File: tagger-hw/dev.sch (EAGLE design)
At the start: 40 parts, among them IC1 4010D, IC2 LP298XS, J1 SMARTPRJ_MYCON2_USB-MINI-B, X1 MICROSD, X2 22-23-2021, X3 22-23-2021

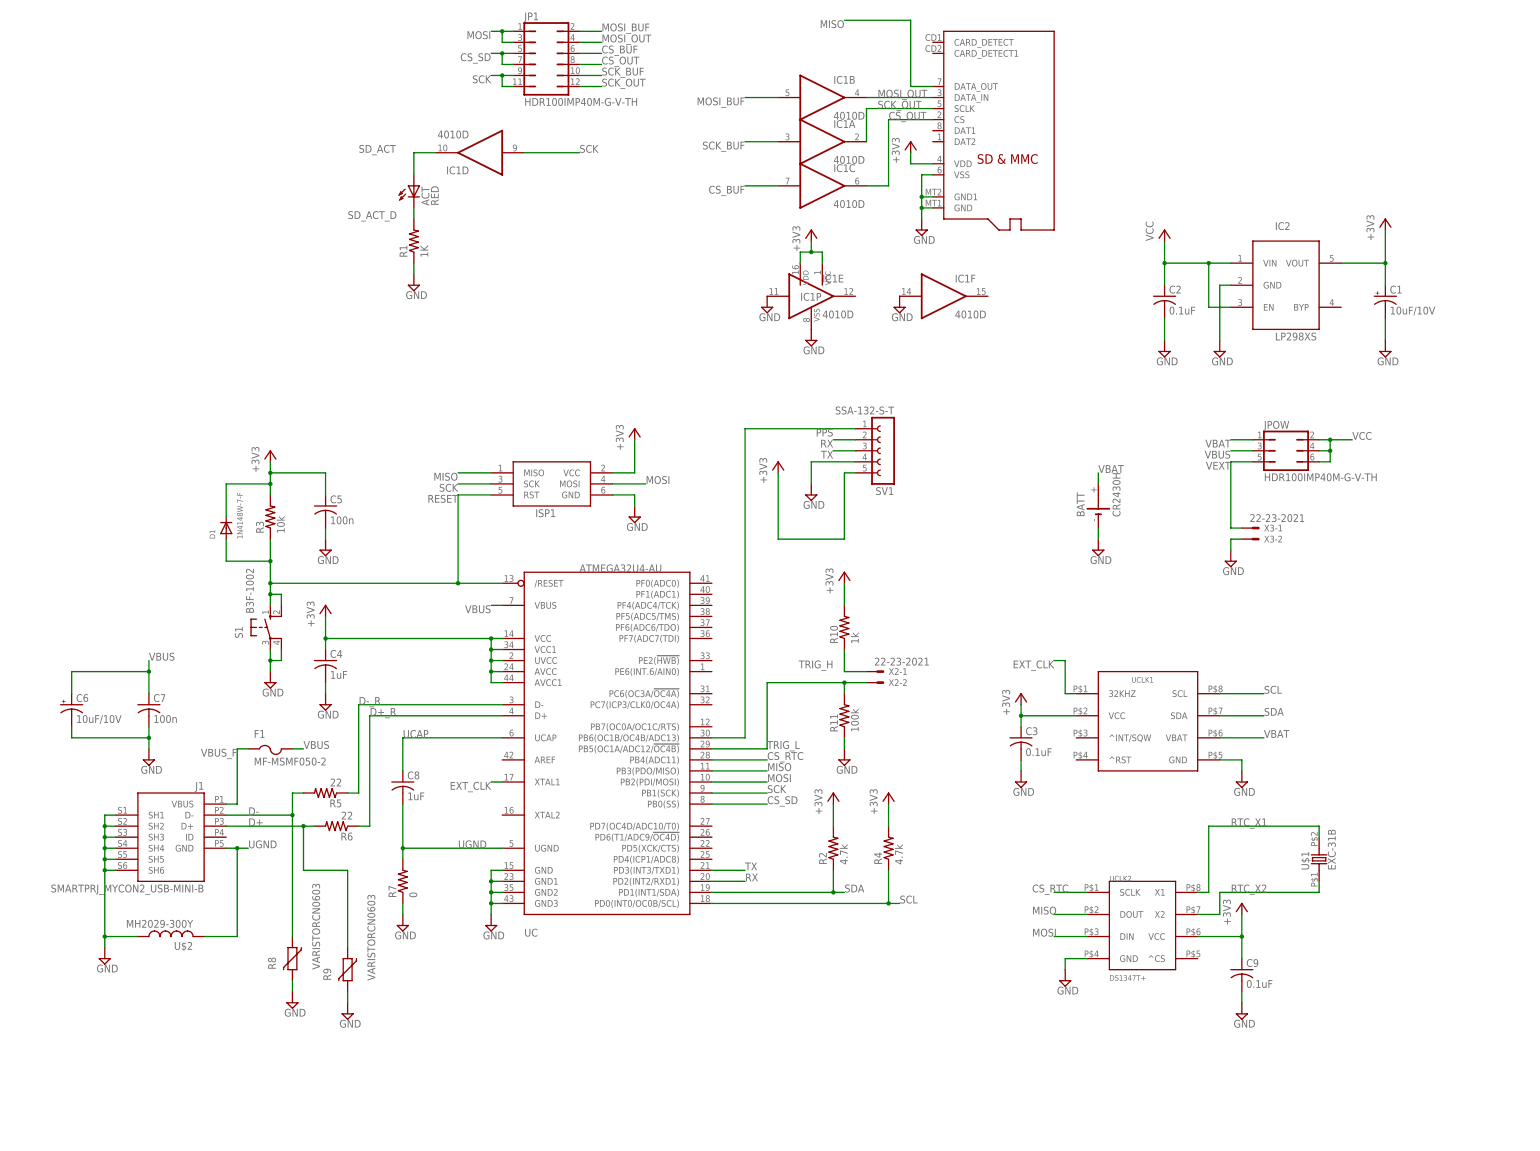
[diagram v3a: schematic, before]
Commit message: Just kidding, add more buttons and LEDs
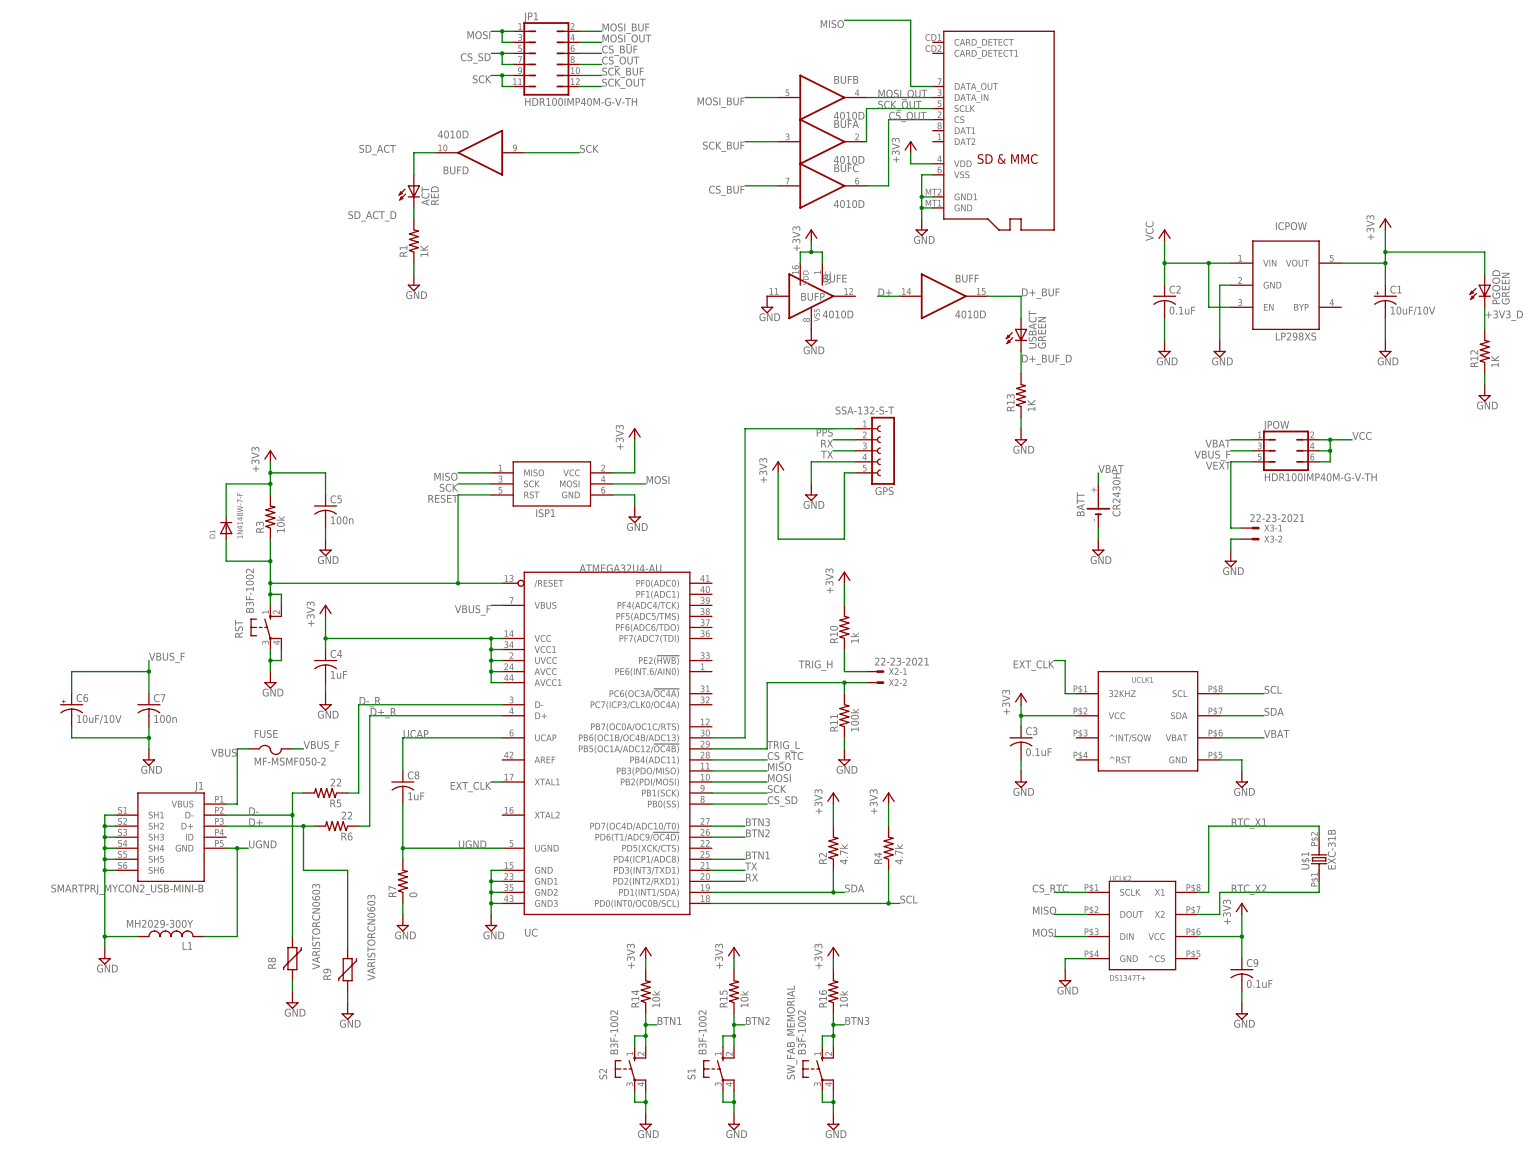
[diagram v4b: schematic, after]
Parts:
- added PGOOD, USBACT: GREEN, adafruit:LEDCHIP-LED0805
- added R12, R13: 1K, adafruit:R-US_R0805
- added R14, R15, R16: 10k, resistor:R-US_R0603
- added RST, S2, SW_FAB_MEMORIAL: B3F-1002, switch-omron:10-XX
- renumbered F1 to FUSE, IC1 to BUF, IC2 to ICPOW, SV1 to GPS, U$2 to L1, X1 to SD
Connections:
- new net +3V3_D: PGOOD.C, R12.2
- new net BTN1: R14.1, S2.S, S2.S1, UC.PD4(ICP1/ADC8)
- new net BTN2: R15.1, S1.S, S1.S1, UC.PD6(T1/ADC9/!OC4D)
- new net BTN3: R16.1, SW_FAB_MEMORIAL.S, SW_FAB_MEMORIAL.S1, UC.PD7(OC4D/ADC10/T0)
- new net D+_BUF: BUFF.O, USBACT.A
- new net D+_BUF_D: R13.2, USBACT.C
- net +3V3: now also PGOOD.A, R14.2, R15.2, R16.2
- net D+: now also BUFF.I
- net GND: now also R12.1, R13.1, RST.P, RST.P1, S2.P, S2.P1, SW_FAB_MEMORIAL.P, SW_FAB_MEMORIAL.P1; no longer BUFF.I
- net RESET: now also RST.S, RST.S1; no longer S1.S, S1.S1
- net VBUS: now also FUSE.1, J1.VBUS; no longer C6.+, C7.1, FUSE.2, JPOW.3, UC.VBUS
- net VBUS_F: now also C6.+, C7.1, FUSE.2, JPOW.3, UC.VBUS; no longer FUSE.1, J1.VBUS
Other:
- moved on the sheet: S1

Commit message: Minor name changes
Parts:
- renumbered U$1 to X1, X2 to J2, X3 to J3
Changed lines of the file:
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@@
 <part name="SUPPLY23" library="supply2" library_urn="urn:adsk.eagle:library:372" deviceset="GND" device=""/>
 <part name="+3V10" library="supply1" library_urn="urn:adsk.eagle:library:371" deviceset="+3V3" device=""/>
-<part name="U$1" library="dorskyee" deviceset="EXC-31B" device=""/>
-<part name="X2" library="con-molex" library_urn="urn:adsk.eagle:library:165" deviceset="22-23-2021" device=""/>
+<part name="X1" library="dorskyee" deviceset="EXC-31B" device=""/>
+<part name="J2" library="con-molex" library_urn="urn:adsk.eagle:library:165" deviceset="22-23-2021" device=""/>
 <part name="R10" library="resistor" library_urn="urn:adsk.eagle:library:348" deviceset="R-US_" device="R0603" package3d_urn="urn:adsk.eagle:package:26057/1" value="1k"/>
 <part name="+3V11" library="supply1" library_urn="urn:adsk.eagle:library:371" deviceset="+3V3" device=""/>
 <part name="R11" library="resistor" library_urn="urn:adsk.eagle:library:348" deviceset="R-US_" device="R0603" package3d_urn="urn:adsk.eagle:package:26057/1" value="100k"/>
 <part name="SUPPLY24" library="supply2" library_urn="urn:adsk.eagle:library:372" deviceset="GND" device=""/>
-<part name="X3" library="con-molex" library_urn="urn:adsk.eagle:library:165" deviceset="22-23-2021" device=""/>
+<part name="J3" library="con-molex" library_urn="urn:adsk.eagle:library:165" deviceset="22-23-2021" device=""/>
 <part name="SUPPLY25" library="supply2" library_urn="urn:adsk.eagle:library:372" deviceset="GND" device=""/>
 <part name="L1" library="dorskyee" deviceset="MH2029-300Y" device=""/>
@@
 <instance part="SUPPLY23" gate="GND" x="116.84" y="-129.54"/>
 <instance part="+3V10" gate="G$1" x="116.84" y="-104.14"/>
-<instance part="U$1" gate="G$1" x="134.62" y="-93.98" rot="R90"/>
-<instance part="X2" gate="-1" x="33.02" y="-50.8"/>
-<instance part="X2" gate="-2" x="33.02" y="-53.34"/>
+<instance part="X1" gate="G$1" x="134.62" y="-93.98" rot="R90"/>
+<instance part="J2" gate="-1" x="33.02" y="-50.8"/>
+<instance part="J2" gate="-2" x="33.02" y="-53.34"/>
 <instance part="R10" gate="G$1" x="25.4" y="-40.64" rot="R90"/>
 <instance part="+3V11" gate="G$1" x="25.4" y="-27.94"/>
 <instance part="R11" gate="G$1" x="25.4" y="-60.96" rot="R90"/>
 <instance part="SUPPLY24" gate="GND" x="25.4" y="-71.12"/>
-<instance part="X3" gate="-1" x="119.38" y="-17.78"/>
-<instance part="X3" gate="-2" x="119.38" y="-20.32"/>
+<instance part="J3" gate="-1" x="119.38" y="-17.78"/>
+<instance part="J3" gate="-2" x="119.38" y="-20.32"/>
 <instance part="SUPPLY25" gate="GND" x="114.3" y="-25.4"/>
 <instance part="L1" gate="G$1" x="-129.54" y="-111.76" rot="R90"/>
@@
 </segment>
 <segment>
-<pinref part="X3" gate="-2" pin="S"/>
+<pinref part="J3" gate="-2" pin="S"/>
 <pinref part="SUPPLY25" gate="GND" pin="GND"/>
 <wire x1="116.84" y1="-20.32" x2="114.3" y2="-20.32" width="0.1524" layer="91"/>
@@
 <wire x1="114.3" y1="-2.54" x2="119.38" y2="-2.54" width="0.1524" layer="91"/>
 <label x="114.3" y="-2.54" size="1.778" layer="95" rot="R180"/>
-<pinref part="X3" gate="-1" pin="S"/>
+<pinref part="J3" gate="-1" pin="S"/>
 <wire x1="116.84" y1="-17.78" x2="114.3" y2="-17.78" width="0.1524" layer="91"/>
 <wire x1="114.3" y1="-17.78" x2="114.3" y2="-2.54" width="0.1524" layer="91"/>
@@
 <wire x1="111.76" y1="-106.68" x2="111.76" y2="-101.6" width="0.1524" layer="91"/>
 <wire x1="111.76" y1="-101.6" x2="134.62" y2="-101.6" width="0.1524" layer="91"/>
-<pinref part="U$1" gate="G$1" pin="1"/>
+<pinref part="X1" gate="G$1" pin="1"/>
 <wire x1="134.62" y1="-101.6" x2="134.62" y2="-99.06" width="0.1524" layer="91"/>
 <label x="114.3" y="-101.6" size="1.778" layer="95"/>
@@
 <wire x1="109.22" y1="-101.6" x2="109.22" y2="-86.36" width="0.1524" layer="91"/>
 <wire x1="109.22" y1="-86.36" x2="134.62" y2="-86.36" width="0.1524" layer="91"/>
-<pinref part="U$1" gate="G$1" pin="2"/>
+<pinref part="X1" gate="G$1" pin="2"/>
 <wire x1="134.62" y1="-86.36" x2="134.62" y2="-88.9" width="0.1524" layer="91"/>
 <label x="114.3" y="-86.36" size="1.778" layer="95"/>
@@
 <net name="TRIG_L" class="0">
 <segment>
-<pinref part="X2" gate="-2" pin="S"/>
+<pinref part="J2" gate="-2" pin="S"/>
 <wire x1="30.48" y1="-53.34" x2="25.4" y2="-53.34" width="0.1524" layer="91"/>
 <wire x1="25.4" y1="-53.34" x2="25.4" y2="-55.88" width="0.1524" layer="91"/>
@@
 <segment>
 <pinref part="R10" gate="G$1" pin="1"/>
-<pinref part="X2" gate="-1" pin="S"/>
+<pinref part="J2" gate="-1" pin="S"/>
 <wire x1="30.48" y1="-50.8" x2="25.4" y2="-50.8" width="0.1524" layer="91"/>
 <wire x1="25.4" y1="-50.8" x2="25.4" y2="-45.72" width="0.1524" layer="91"/>

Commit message: More renaming
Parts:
- ICPOW: value LP298XS -> CAT6219-330TDGT3
- renumbered J1 to JUSB
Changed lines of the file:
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@@
 <part name="SUPPLY3" library="supply2" library_urn="urn:adsk.eagle:library:372" deviceset="GND" device=""/>
 <part name="+3V3" library="supply1" library_urn="urn:adsk.eagle:library:371" deviceset="+3V3" device=""/>
-<part name="ICPOW" library="adafruit" deviceset="LP298X" device="S"/>
+<part name="ICPOW" library="adafruit" deviceset="LP298X" device="S" value="CAT6219-330TDGT3"/>
 <part name="P+2" library="supply1" library_urn="urn:adsk.eagle:library:371" deviceset="VCC" device=""/>
 <part name="SUPPLY1" library="supply2" library_urn="urn:adsk.eagle:library:372" deviceset="GND" device=""/>
@@
 <part name="SUPPLY16" library="supply2" library_urn="urn:adsk.eagle:library:372" deviceset="GND" device=""/>
 <part name="JPOW" library="jumper" library_urn="urn:adsk.eagle:library:252" deviceset="JP3Q" device="" package3d_urn="urn:adsk.eagle:package:15460/1" value="HDR100IMP40M-G-V-TH"/>
-<part name="J1" library="dorskyee" deviceset="SMARTPRJ_MYCON2_USB-MINI-B" device=""/>
+<part name="JUSB" library="dorskyee" deviceset="SMARTPRJ_MYCON2_USB-MINI-B" device=""/>
 <part name="SUPPLY17" library="supply2" library_urn="urn:adsk.eagle:library:372" deviceset="GND" device=""/>
 <part name="R5" library="resistor" library_urn="urn:adsk.eagle:library:348" deviceset="R-US_" device="R0603" package3d_urn="urn:adsk.eagle:package:26057/1" value="22"/>
@@
 <instance part="SUPPLY16" gate="GND" x="83.82" y="-22.86"/>
 <instance part="JPOW" gate="B" x="127" y="0" rot="R270"/>
-<instance part="J1" gate="G$1" x="-129.54" y="-86.36" rot="MR0"/>
+<instance part="JUSB" gate="G$1" x="-129.54" y="-86.36" rot="MR0"/>
 <instance part="SUPPLY17" gate="GND" x="-144.78" y="-116.84"/>
 <instance part="R5" gate="G$1" x="-93.98" y="-78.74" rot="R180"/>
@@
 </segment>
 <segment>
-<pinref part="J1" gate="G$1" pin="SH6"/>
+<pinref part="JUSB" gate="G$1" pin="SH6"/>
 <pinref part="SUPPLY17" gate="GND" pin="GND"/>
 <wire x1="-142.24" y1="-96.52" x2="-144.78" y2="-96.52" width="0.1524" layer="91"/>
 <wire x1="-144.78" y1="-96.52" x2="-144.78" y2="-111.76" width="0.1524" layer="91"/>
-<pinref part="J1" gate="G$1" pin="SH5"/>
+<pinref part="JUSB" gate="G$1" pin="SH5"/>
 <wire x1="-144.78" y1="-111.76" x2="-144.78" y2="-114.3" width="0.1524" layer="91"/>
 <wire x1="-142.24" y1="-93.98" x2="-144.78" y2="-93.98" width="0.1524" layer="91"/>
 <wire x1="-144.78" y1="-93.98" x2="-144.78" y2="-96.52" width="0.1524" layer="91"/>
 <junction x="-144.78" y="-96.52"/>
-<pinref part="J1" gate="G$1" pin="SH4"/>
+<pinref part="JUSB" gate="G$1" pin="SH4"/>
 <wire x1="-142.24" y1="-91.44" x2="-144.78" y2="-91.44" width="0.1524" layer="91"/>
 <wire x1="-144.78" y1="-91.44" x2="-144.78" y2="-93.98" width="0.1524" layer="91"/>
 <junction x="-144.78" y="-93.98"/>
-<pinref part="J1" gate="G$1" pin="SH3"/>
+<pinref part="JUSB" gate="G$1" pin="SH3"/>
 <wire x1="-142.24" y1="-88.9" x2="-144.78" y2="-88.9" width="0.1524" layer="91"/>
 <wire x1="-144.78" y1="-88.9" x2="-144.78" y2="-91.44" width="0.1524" layer="91"/>
 <junction x="-144.78" y="-91.44"/>
-<pinref part="J1" gate="G$1" pin="SH2"/>
+<pinref part="JUSB" gate="G$1" pin="SH2"/>
 <wire x1="-142.24" y1="-86.36" x2="-144.78" y2="-86.36" width="0.1524" layer="91"/>
 <wire x1="-144.78" y1="-86.36" x2="-144.78" y2="-88.9" width="0.1524" layer="91"/>
 <junction x="-144.78" y="-88.9"/>
-<pinref part="J1" gate="G$1" pin="SH1"/>
+<pinref part="JUSB" gate="G$1" pin="SH1"/>
 <wire x1="-142.24" y1="-83.82" x2="-144.78" y2="-83.82" width="0.1524" layer="91"/>
 <wire x1="-144.78" y1="-83.82" x2="-144.78" y2="-86.36" width="0.1524" layer="91"/>
@@
 <net name="D-" class="0">
 <segment>
-<pinref part="J1" gate="G$1" pin="D-"/>
+<pinref part="JUSB" gate="G$1" pin="D-"/>
 <label x="-111.76" y="-83.82" size="1.778" layer="95"/>
 <pinref part="R5" gate="G$1" pin="2"/>
@@
 <net name="D+" class="0">
 <segment>
-<pinref part="J1" gate="G$1" pin="D+"/>
+<pinref part="JUSB" gate="G$1" pin="D+"/>
 <label x="-111.76" y="-86.36" size="1.778" layer="95"/>
 <pinref part="R6" gate="G$1" pin="2"/>
@@
 <net name="UGND" class="0">
 <segment>
-<pinref part="J1" gate="G$1" pin="GND"/>
+<pinref part="JUSB" gate="G$1" pin="GND"/>
 <wire x1="-116.84" y1="-91.44" x2="-114.3" y2="-91.44" width="0.1524" layer="91"/>
 <label x="-111.76" y="-91.44" size="1.778" layer="95"/>
@@
 <net name="VBUS" class="0">
 <segment>
-<pinref part="J1" gate="G$1" pin="VBUS"/>
+<pinref part="JUSB" gate="G$1" pin="VBUS"/>
 <wire x1="-116.84" y1="-81.28" x2="-114.3" y2="-81.28" width="0.1524" layer="91"/>
 <wire x1="-114.3" y1="-81.28" x2="-114.3" y2="-68.58" width="0.1524" layer="91"/>
